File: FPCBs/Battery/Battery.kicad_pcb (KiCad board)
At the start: 2 copper layers, 20.5 x 23 mm, 6 parts

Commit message: Battery fpcb
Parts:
- moved Power_Connector_Camera1 1.06 mm to (139.7, 91.7)
- moved F1 0.93 mm to (137.0, 88.1)
- moved R1 0.93 mm to (140.5, 88.1)
- moved C1 0.93 mm to (138.3, 88.1)
- moved C2 0.93 mm to (139.3, 88.1)
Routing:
- net Net-(Power_Connector_Battery1-+): track 12.5 -> 14.1 mm
- net Net-(Power_Connector_Battery1--): track 26.3 -> 25.4 mm
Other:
- board size 20.5 x 23 mm -> 21.8 x 23.7 mm
- board text added: "+"
- board text added: "-"

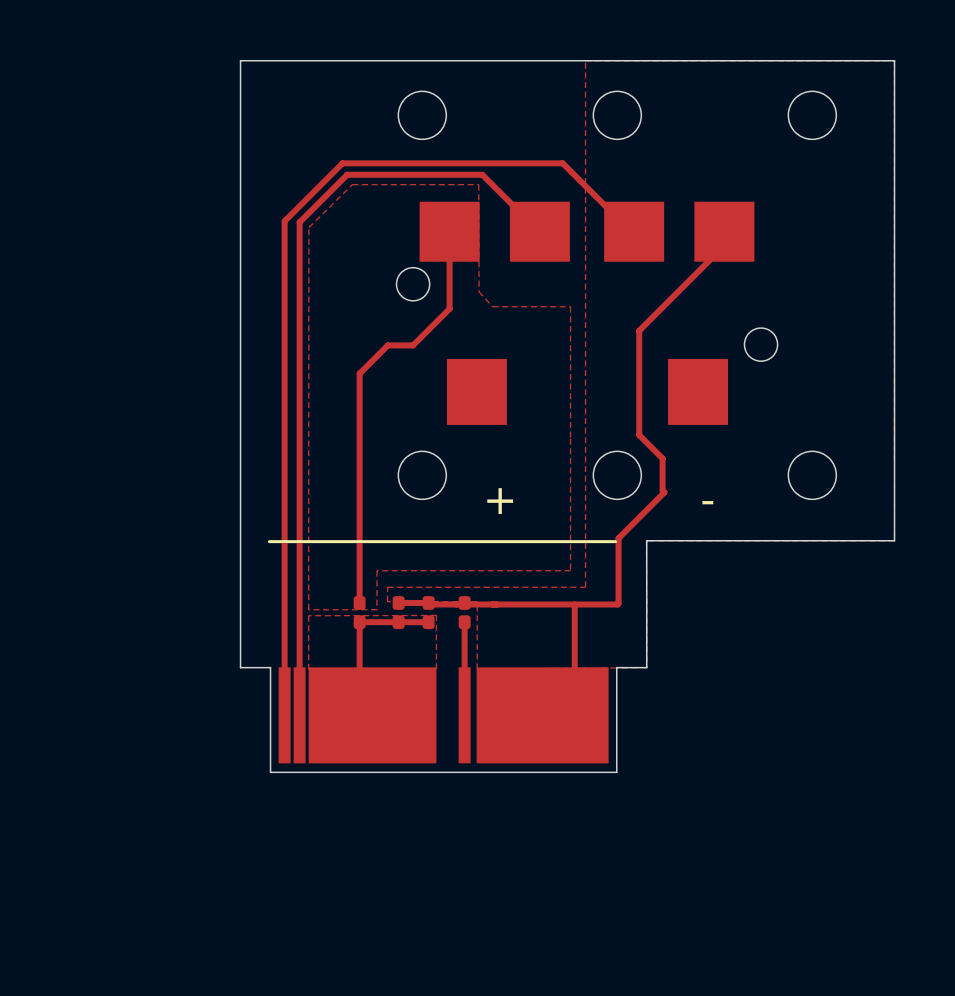
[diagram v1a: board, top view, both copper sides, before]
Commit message: Add pad mask
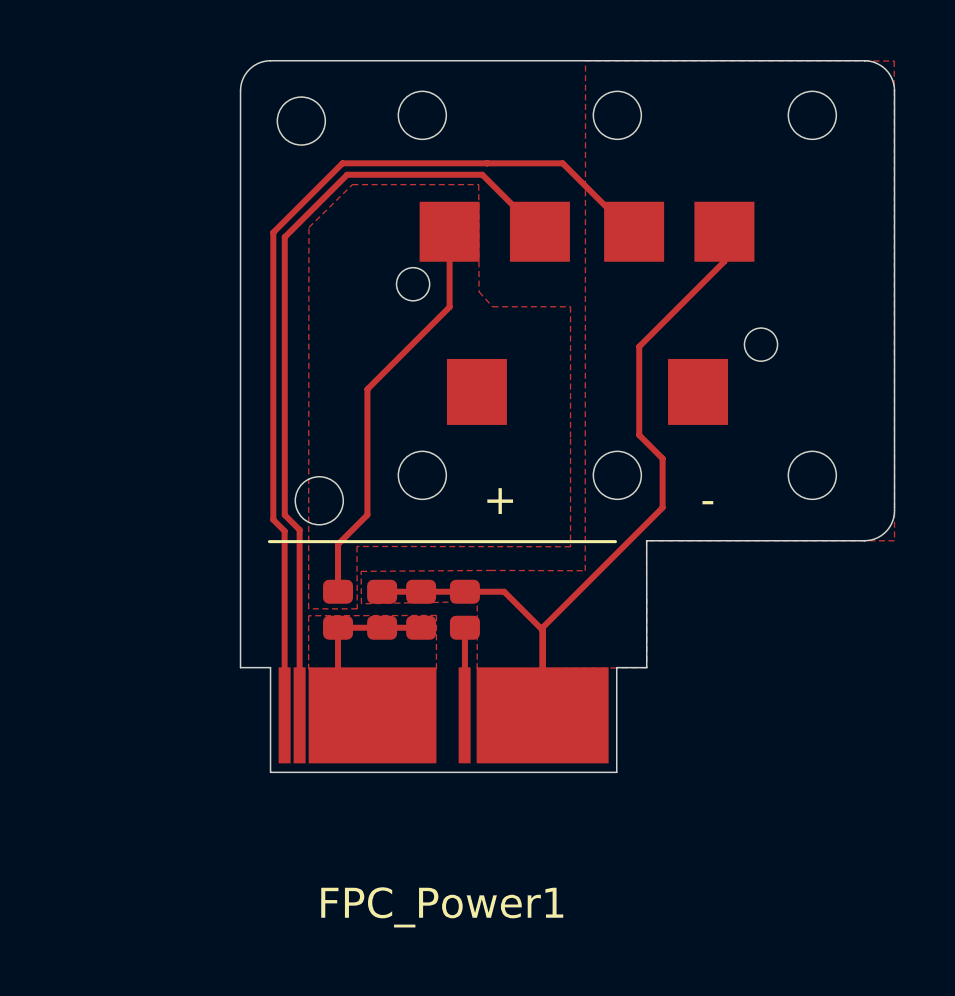
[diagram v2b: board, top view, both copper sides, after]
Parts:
- C1, C2: footprint Capacitor_SMD:C_0201_0603Metric -> Leica-G9ii:R_2x1mm
- Connector_Battery1: renamed from Power_Connector_Battery1; footprint Leica-G9ii:Power_Connector_Battery -> Leica-G9ii:Connector_Battery
- F1, R1: footprint Resistor_SMD:R_0201_0603Metric -> Leica-G9ii:R_2x1mm
- FPC_Power1: renamed from Power_Connector_Camera1; footprint Leica-G9ii:Power_Connector_Camera -> Leica-G9ii:FPC_Power
- moved F1 0.73 mm to (136.2, 88.0)
- moved C1 0.56 mm to (137.7, 88.0)
- moved C2 0.27 mm to (139.0, 88.0)
- moved R1 0.10 mm to (140.5, 88.0)
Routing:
- net Net-(Connector_Battery1--): track 25.4 -> 28.1 mm
- net Net-(FPC_Power1-+): track 5.63 -> 6.30 mm
- net Net-(Connector_Battery1-+): track 14.1 -> 13.5 mm
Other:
- outline, holes or cut-outs redrawn

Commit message: Add masks to the battery pcb
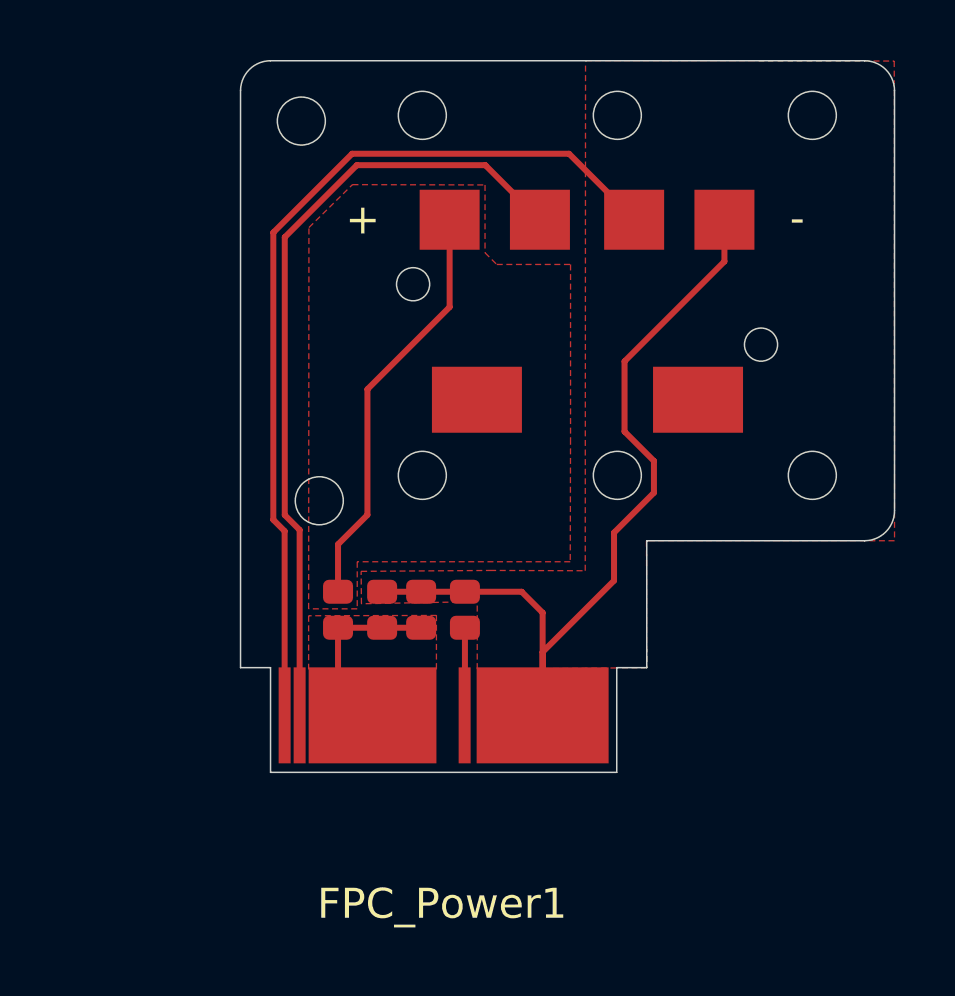
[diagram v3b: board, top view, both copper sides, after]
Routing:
- net Net-(Connector_Battery1--): track 28.1 -> 28.6 mm

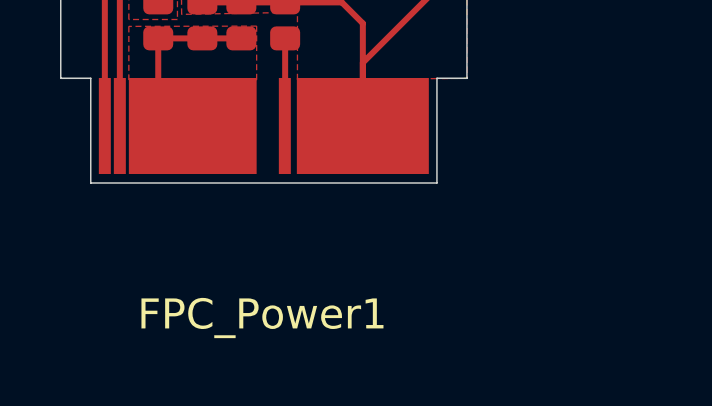
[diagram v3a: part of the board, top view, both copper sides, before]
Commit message: Add EVF extender FPCB
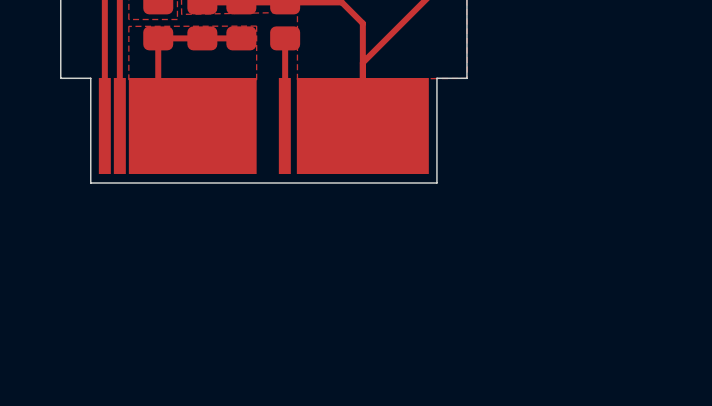
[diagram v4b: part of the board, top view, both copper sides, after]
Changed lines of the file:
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@@
 			(unlocked yes)
 			(layer "F.SilkS")
+			(hide yes)
 			(effects
 				(font

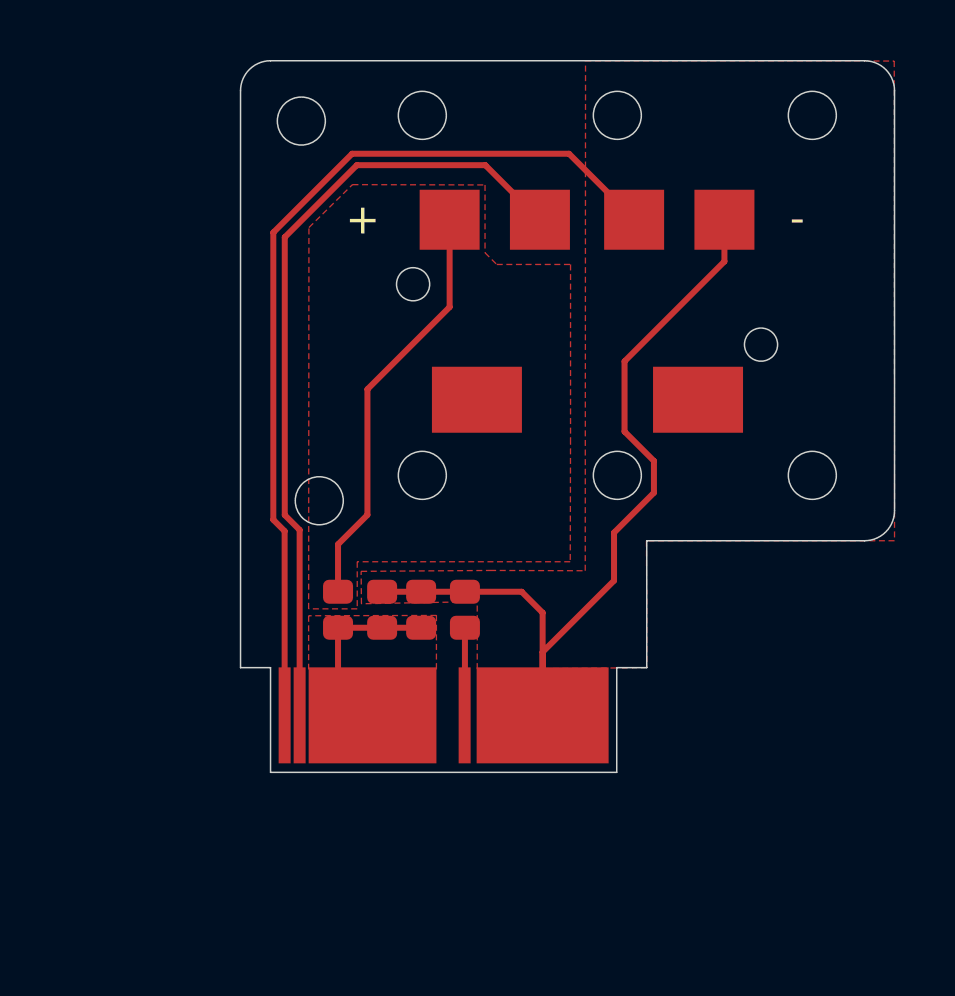
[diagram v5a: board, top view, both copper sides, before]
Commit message: Fix battery fpc size
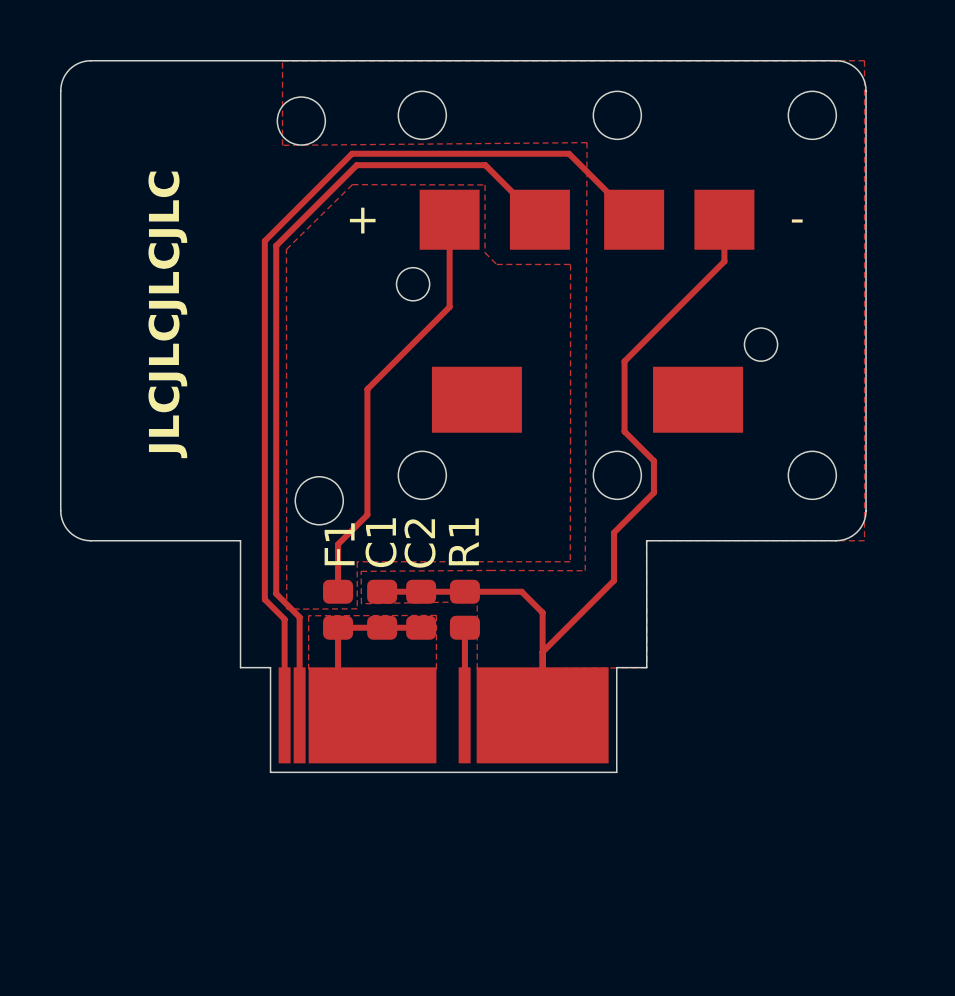
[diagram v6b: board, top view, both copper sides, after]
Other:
- board size 21.8 x 23.7 mm -> 26.8 x 23.7 mm
- board text added: "JLCJLCJLCJLC"
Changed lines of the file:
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@@
 		(tags "resistor")
 		(property "Reference" "C1"
-			(at 1.83 -0.02 90)
+			(at -2.26 0 90)
 			(layer "F.SilkS")
-			(hide yes)
 			(effects
 				(font
@@
 		(tags "resistor")
 		(property "Reference" "F1"
-			(at 0 -1.43 90)
+			(at 2.18 0.09 90)
 			(layer "F.SilkS")
-			(hide yes)
 			(effects
 				(font
@@
 		(tags "resistor")
 		(property "Reference" "R1"
-			(at -1.83 0.05 90)
+			(at 2.26 0 90)
 			(layer "F.SilkS")
-			(hide yes)
 			(effects
 				(font
@@
 		(tags "resistor")
 		(property "Reference" "C2"
-			(at 1.89 -0.02 90)
+			(at -2.24 0 90)
 			(layer "F.SilkS")
-			(hide yes)
 			(effects
 				(font
@@
 		)
 		(property "Value" "~"
-			(at 0.02 7.61 0)
+			(at -0.04 2.815 0)
 			(unlocked yes)
 			(layer "F.Fab")
+			(hide yes)
 			(effects
 				(font
@@
 		)
 		(fp_text user "${REFERENCE}"
-			(at 0.02 9.11 0)
+			(at 0.07 4.305 0)
 			(unlocked yes)
 			(layer "F.Fab")
@@
 	)
 	(gr_arc
-		(start 154.8 84.7)
-		(mid 154.507107 85.407107)
-		(end 153.8 85.7)
-		(stroke
-			(width 0.05)
-			(type default)
+		(start 153.85 84.7)
+		(mid 153.557107 85.407107)
+		(end 152.85 85.7)
+		(stroke
+			(width 0.05)
+			(type default)
+		)
+		(layer "Edge.Cuts")
+	)
+	(gr_line
+		(start 127.007107 70.7)
+		(end 127.007107 84.7)
+		(stroke
+			(width 0.05)
+			(type solid)
 		)
 		(layer "Edge.Cuts")
 	)
 	(gr_arc
-		(start 153.8 69.7)
-		(mid 154.507107 69.992893)
-		(end 154.8 70.7)
+		(start 152.85 69.7)
+		(mid 153.557107 69.992893)
+		(end 153.85 70.7)
+		(stroke
+			(width 0.05)
+			(type default)
+		)
+		(layer "Edge.Cuts")
+	)
+	(gr_arc
+		(start 128.007107 85.7)
+		(mid 127.3 85.407107)
+		(end 127.007107 84.7)
 		(stroke
 			(width 0.05)
@@
 	)
 	(gr_line
-		(start 153.8 85.7)
+		(start 152.85 85.7)
 		(end 146.54 85.7)
 		(stroke
@@
 			(width 0.05)
 			(type default)
+		)
+		(layer "Edge.Cuts")
+	)
+	(gr_line
+		(start 133 85.7)
+		(end 128.007107 85.7)
+		(stroke
+			(width 0.05)
+			(type solid)
 		)
 		(layer "Edge.Cuts")
@@
 	)
 	(gr_line
-		(start 154.8 84.7)
-		(end 154.8 70.7)
-		(stroke
-			(width 0.05)
-			(type default)
+		(start 153.85 84.7)
+		(end 153.85 70.7)
+		(stroke
+			(width 0.05)
+			(type solid)
 		)
 		(layer "Edge.Cuts")
@@
 	)
 	(gr_line
-		(start 133 70.7)
+		(start 133 85.7)
 		(end 133 89.93)
 		(stroke
@@
 	)
 	(gr_arc
-		(start 133 70.7)
-		(mid 133.292893 69.992893)
-		(end 134 69.7)
+		(start 127.007107 70.7)
+		(mid 127.3 69.992893)
+		(end 128.007107 69.7)
 		(stroke
 			(width 0.05)
@@
 	)
 	(gr_line
-		(start 153.8 69.7)
-		(end 134 69.7)
+		(start 152.85 69.7)
+		(end 128.007107 69.7)
 		(stroke
 			(width 0.05)
@@
 		(layer "User.9")
 	)
+	(gr_arc
+		(start 128.007107 85.7)
+		(mid 127.299996 85.407109)
+		(end 127.007107 84.7)
+		(stroke
+			(width 0.05)
+			(type default)
+		)
+		(layer "User.9")
+	)
 	(gr_circle
 		(center 152.06 71.52)
@@
 		(layer "User.9")
 	)
+	(gr_line
+		(start 127.007107 70.700004)
+		(end 127.007107 84.7)
+		(stroke
+			(width 0.05)
+			(type solid)
+		)
+		(layer "User.9")
+	)
 	(gr_circle
 		(center 138.75 77.15)
@@
 	)
 	(gr_line
-		(start 153.8 69.7)
-		(end 134 69.7)
+		(start 152.85 69.7)
+		(end 128.007107 69.7)
 		(stroke
 			(width 0.05)
@@
 	)
 	(gr_arc
-		(start 153.8 69.7)
-		(mid 154.507107 69.992893)
-		(end 154.8 70.7)
-		(stroke
-			(width 0.05)
-			(type default)
-		)
-		(layer "User.9")
-	)
-	(gr_line
-		(start 133 70.7)
+		(start 152.85 69.7)
+		(mid 153.557107 69.992893)
+		(end 153.85 70.7)
+		(stroke
+			(width 0.05)
+			(type default)
+		)
+		(layer "User.9")
+	)
+	(gr_line
+		(start 133 85.7)
 		(end 133 89.93)
 		(stroke
@@
 	)
 	(gr_arc
-		(start 154.8 84.7)
-		(mid 154.507107 85.407107)
-		(end 153.8 85.7)
-		(stroke
-			(width 0.05)
-			(type default)
-		)
-		(layer "User.9")
-	)
-	(gr_line
-		(start 154.8 84.7)
-		(end 154.8 70.7)
+		(start 153.85 84.7)
+		(mid 153.557107 85.407107)
+		(end 152.85 85.7)
+		(stroke
+			(width 0.05)
+			(type default)
+		)
+		(layer "User.9")
+	)
+	(gr_line
+		(start 153.85 84.7)
+		(end 153.85 70.7)
 		(stroke
 			(width 0.05)
@@
 	)
 	(gr_line
-		(start 153.8 85.7)
+		(start 152.85 85.7)
 		(end 146.54 85.7)
 		(stroke
@@
 	)
 	(gr_arc
-		(start 133 70.7)
-		(mid 133.292893 69.992893)
-		(end 134 69.7)
-		(stroke
-			(width 0.05)
-			(type default)
+		(start 127.007107 70.700004)
+		(mid 127.3 69.992897)
+		(end 128.007107 69.700004)
+		(stroke
+			(width 0.05)
+			(type default)
+		)
+		(layer "User.9")
+	)
+	(gr_line
+		(start 133 85.7)
+		(end 128.007107 85.7)
+		(stroke
+			(width 0.05)
+			(type solid)
 		)
 		(layer "User.9")
@@
 		)
 	)
+	(gr_text "JLCJLCJLCJLC"
+		(at 131.07 82.87 90)
+		(layer "F.SilkS")
+		(effects
+			(font
+				(size 1 1)
+				(thickness 0.18)
+				(bold yes)
+			)
+			(justify left bottom)
+		)
+	)
 	(gr_text "-"
 		(at 151.31 75.54 0)
@@
 	)
 	(segment
-		(start 134.093 75.425586)
+		(start 133.81 75.708586)
 		(end 136.718586 72.8)
 		(width 0.2)
@@
 	)
 	(segment
-		(start 134.47 91.52)
-		(end 134.47 85.378575)
+		(start 136.718586 72.8)
+		(end 143.95 72.8)
 		(width 0.2)
 		(layer "F.Cu")
@@
 	)
 	(segment
-		(start 134.47 85.378575)
-		(end 134.093 85.001575)
+		(start 134.47 91.52)
+		(end 134.47 88.32)
+		(width 0.2)
+		(layer "F.Cu")
+		(net 4)
+	)
+	(segment
+		(start 134.47 88.32)
+		(end 133.81 87.66)
+		(width 0.2)
+		(layer "F.Cu")
+		(net 4)
+	)
+	(segment
+		(start 133.81 87.66)
+		(end 133.81 75.708586)
 		(width 0.2)
 		(layer "F.Cu")
@@
 	)
 	(segment
-		(start 134.093 85.001575)
-		(end 134.093 75.425586)
-		(width 0.2)
-		(layer "F.Cu")
-		(net 4)
-	)
-	(segment
-		(start 136.718586 72.8)
-		(end 143.95 72.8)
-		(width 0.2)
-		(layer "F.Cu")
-		(net 4)
-	)
-	(segment
-		(start 134.474 75.583402)
+		(start 134.19 87.47)
+		(end 134.19 75.867402)
+		(width 0.2)
+		(layer "F.Cu")
+		(net 5)
+	)
+	(segment
+		(start 134.19 75.867402)
 		(end 136.876402 73.181)
 		(width 0.2)
@@
 	(segment
 		(start 134.97 91.52)
-		(end 134.97 85.33976)
-		(width 0.2)
-		(layer "F.Cu")
-		(net 5)
-	)
-	(segment
-		(start 134.474 84.84376)
-		(end 134.474 75.583402)
+		(end 134.97 88.25)
 		(width 0.2)
 		(layer "F.Cu")
@@
 	)
 	(segment
-		(start 134.97 85.33976)
-		(end 134.474 84.84376)
+		(start 134.97 88.25)
+		(end 134.19 87.47)
 		(width 0.2)
 		(layer "F.Cu")
@@
 		(polygon
 			(pts
-				(xy 154.79 69.71) (xy 154.8 85.7) (xy 146.53 85.7) (xy 146.55 89.93) (xy 145.53 89.94) (xy 140.89 89.98)
-				(xy 140.89 87.73) (xy 137.03 87.8) (xy 137.02 86.72) (xy 141.32 86.69) (xy 144.49 86.7) (xy 144.5 69.7)
+				(xy 153.8 69.7) (xy 153.8 85.7) (xy 146.53 85.7) (xy 146.55 89.93) (xy 145.53 89.94) (xy 140.89 89.98)
+				(xy 140.89 87.73) (xy 137.03 87.8) (xy 137.02 86.72) (xy 141.32 86.69) (xy 144.49 86.7) (xy 144.55 72.43)
+				(xy 134.4 72.52) (xy 134.4 69.71)
 			)
 		)
@@
 			(pts
 				(xy 141.15 76.1) (xy 141.54 76.49) (xy 144 76.49) (xy 144 82.3) (xy 143.99 86.4) (xy 136.89 86.4)
-				(xy 136.89 87.97) (xy 135.27 87.97) (xy 135.28 75.26) (xy 136.73 73.83) (xy 141.15 73.84)
-			)
-		)
+				(xy 136.89 87.97) (xy 134.54 87.98) (xy 134.53 75.99) (xy 136.73 73.83) (xy 141.15 73.84)
+			)
+		)
